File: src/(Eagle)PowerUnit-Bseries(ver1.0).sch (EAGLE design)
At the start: 84 parts, among them CON1 XT90PW-M, CON2 XT90PW-F, CON3 XT60PW-F, CON4 XT60PW-F, CON5 XT60PW-F, CON6 XT60PW-F, Q1 DMP3056L-7, Q3 DMP3056L-7, U1 LQFP64, U2 MCP2517FD, U3 CH340E, U4 AP63203WU-7, U5 AP63205WU-7, U6 AP331AWG-7, U8 AP331AWG-7

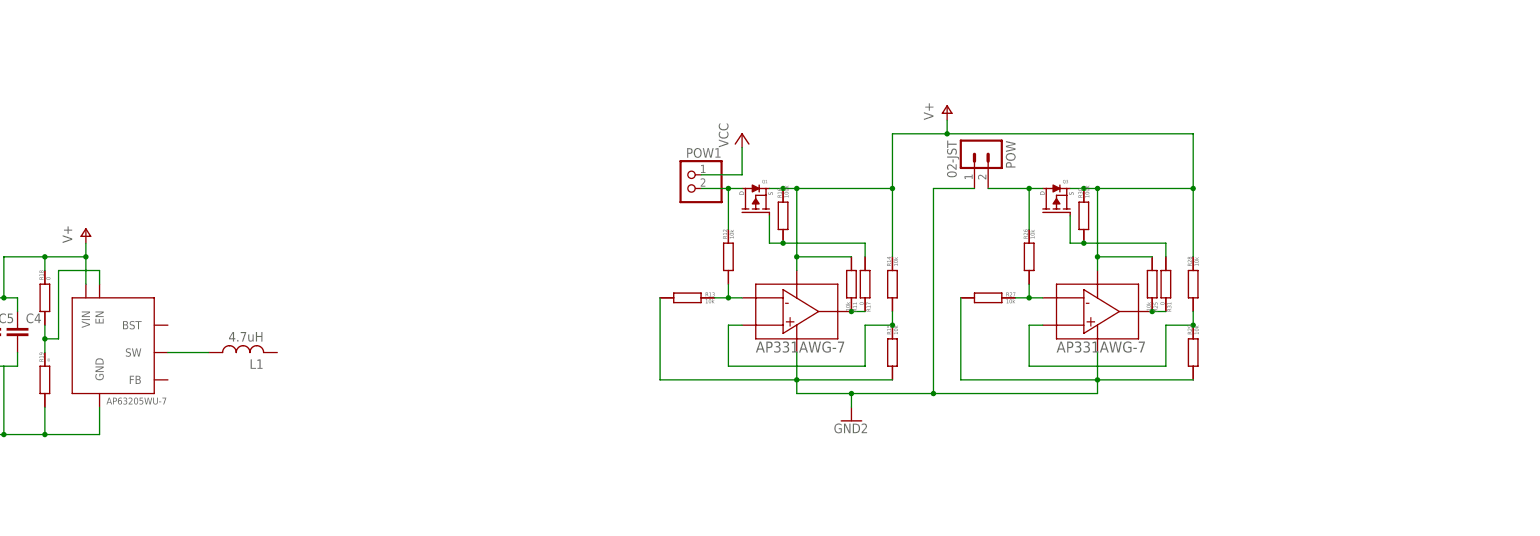
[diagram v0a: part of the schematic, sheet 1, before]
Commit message: 5VDCDCの出力コンをOSコンにした
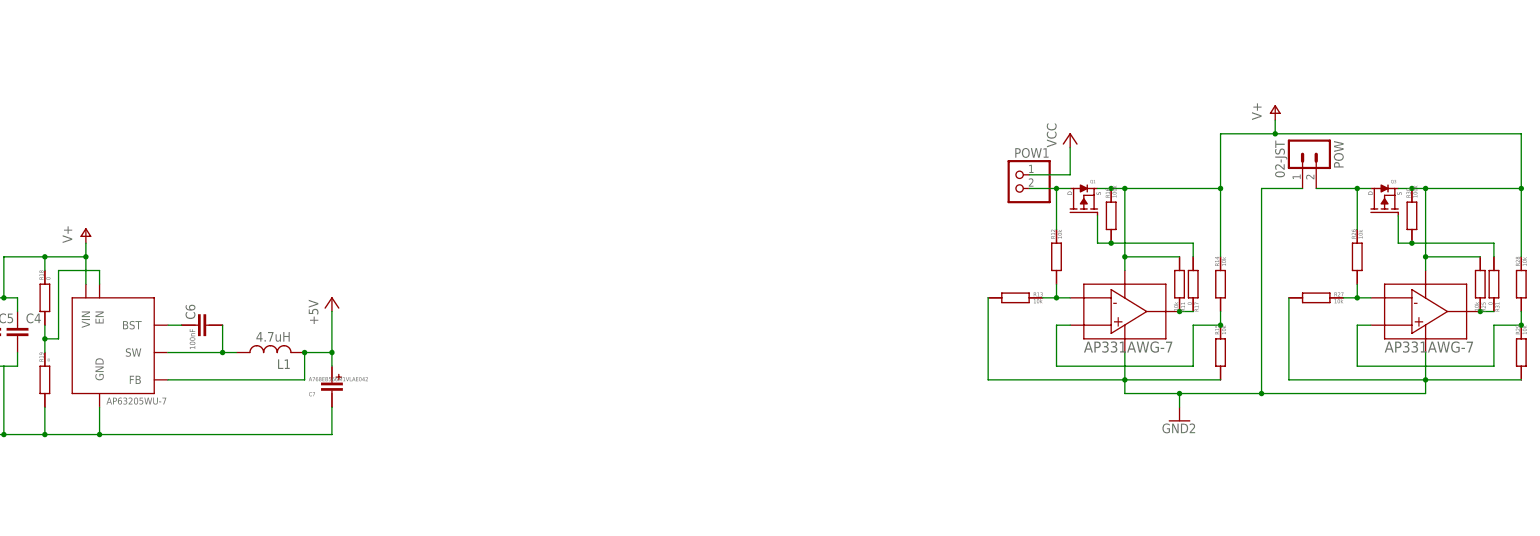
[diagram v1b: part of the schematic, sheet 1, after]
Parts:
- added C6: GCM188L81H104KA57, GCM188L81H104K57(0.1uF):GCM188L81H104KA57
- added C7: A768EB566M1VLAE042, A768EB566M1VLAE042:A768EB566M1VLAE042
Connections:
- new net +5V: C7.ANODE, L1.R, U5.FB
- new net N$41: C6.P$1, U5.BST
- net GND2: now also C7.CATHODE
- net N$40: now also C6.P$2
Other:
- moved on the sheet: L1, POW, POW1, Q1, Q3, R11, R12, R13, R14, R15, R16, R17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

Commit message: +5V周りの冗長性を高める回路を構成(大晦日ですよ？（笑）)
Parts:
- added C8: GCM188L81H104KA57, GCM188L81H104K57(0.1uF):GCM188L81H104KA57
- added Q2, Q4: SSM3J332R, SSM3J332R:SSM3J332R
- added R20, R21, R22, R23, R24, R34, R35, R36, R37, R38: 10k, CR0603:CR0603
- added R32, R39: 100k, CR0603:CR0603
- added R33, R40: 0, CR0603:CR0603
- added U7, U9: AP331AWG-7, AP331AWG-7:AP331AWG-7
- R18: value 0 -> 12k
- R19: value ∞ -> 3k
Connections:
- new net N$43: Q2.GATE, R20.RIGHT, R32.LEFT, R33.LEFT, R33.RIGHT, U7.OUTPUT
- new net N$44: R21.LEFT, R22.RIGHT, U7.IN-
- new net N$47: R23.LEFT, R24.RIGHT, U7.IN+
- new net N$51: Q4.GATE, R34.RIGHT, R39.LEFT, R40.LEFT, R40.RIGHT, U9.OUTPUT
- new net N$52: R35.LEFT, R36.RIGHT, U9.IN-
- new net N$53: R37.LEFT, R38.RIGHT, U9.IN+
- new net N$55: C7.ANODE, L1.R, Q2.DRAIN, R21.RIGHT, U5.FB
- net +5V: now also Q2.SOURCE, Q4.SOURCE, R20.LEFT, R23.RIGHT, R32.RIGHT, R34.LEFT, R37.RIGHT, R39.RIGHT, U7.VCC, U9.VCC; no longer C7.ANODE, L1.R, U5.FB
- net GND2: now also C8.P$2, R22.LEFT, R24.LEFT, R36.LEFT, R38.LEFT, U7.GND, U9.GND
- net U5V: now also Q4.DRAIN, R35.RIGHT
- net V+: now also C8.P$1
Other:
- moved on the sheet: C4, C5, GND, POW, POW1, Q1, Q3, R11, R12, R13, R14, R15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

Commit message: CANコントローラのXtal選定
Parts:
- removed JP2: (no value), pinhead:PINHD-1X2
- removed Q1, Q3: DMP3056L-7, DMP3056L-7:DMP3056L-7
- removed R11, R12, R13, R14, R15, R25, R26, R27, R28, R29: 10k, CR0603:CR0603
- removed R16, R30: 100k, CR0603:CR0603
- removed R17, R31: 0, CR0603:CR0603
- removed U4: AP63203WU-7, AP63203WU-7:AP63203WU-7
- removed U6, U8: AP331AWG-7, AP331AWG-7:AP331AWG-7
- added C10, C11, C13: GCM188L81H104KA57, GCM188L81H104K57(0.1uF):GCM188L81H104KA57
- added C12, C9: GRM32ER71E226KE15, GRM32ER71E226KE15:GRM32ER71E226KE15
- added D1, D2: GS1010FL, GS1010FL:GS1010FL
- added SW1: SS-12SDP2, SS-12SDP2:SS-12SDP2
- added U$4: AZ1117CH-3.3TRG1, AZ1117CH-3.3TRG1:AZ1117CH-3.3TRG1
- added X1: XRCGB40M000F4M00R0, XRCGB40M000F4M00R0:XRCGB40M000F4M00R0
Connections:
- removed net N$38 (its old number): R12.LEFT, R13.RIGHT, U6.IN-
- removed net N$45: POW.2, Q3.DRAIN, R26.RIGHT
- removed net N$46: Q3.GATE, R25.RIGHT, R30.LEFT, R31.LEFT, R31.RIGHT, U8.OUTPUT
- removed net N$48: R26.LEFT, R27.RIGHT, U8.IN-
- removed net N$49: R28.LEFT, R29.RIGHT, U8.IN+
- new net CS: U1.P33, U2.NCS
- new net MISO: U1.P35, U2.SDO
- new net MOSI: U1.P36, U2.SDI
- new net N$42: U2.OSC2, X1.1
- new net SCK: U1.P34, U2.SCK
- net +3V3: now also C11.P$1, C12.1, C13.P$2, U$1.VIO, U$4.OUTPUT, U2.VDD
- net +5V: now also C10.P$1, C9.1, U$1.VDD, U$4.INPUT
- net CANL: now also SW1.C; no longer JP2.2
- net GND: no longer U$1.VSS, U2.VSS
- net GND2: now also C10.P$2, C11.P$2, C12.2, C13.P$1, C9.2, U$1.VSS, U$4.GND, U2.VSS; no longer R13.LEFT, R15.LEFT, R27.LEFT, R29.LEFT, U4.GND, U6.GND, U8.GND
- net N$23: now also SW1.R; no longer JP2.1
- net N$35: now also D1.A; no longer Q1.DRAIN, R12.RIGHT
- net N$37: now also D2.A, POW.2; no longer Q1.GATE, R11.RIGHT, R16.LEFT, R17.LEFT, R17.RIGHT, U6.OUTPUT
- net N$39: now also U2.OSC1, X1.2; no longer R14.LEFT, R15.RIGHT, U6.IN+
- net V+: now also D1.C, D2.C; no longer Q1.SOURCE, Q3.SOURCE, R11.LEFT, R14.RIGHT, R16.RIGHT, R25.LEFT, R28.RIGHT, R30.RIGHT, U6.VCC, U8.VCC
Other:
- moved on the sheet: C3, C4, C5, C6, C7, C8, ECHO, GND, L1, LED4, POW, POW1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

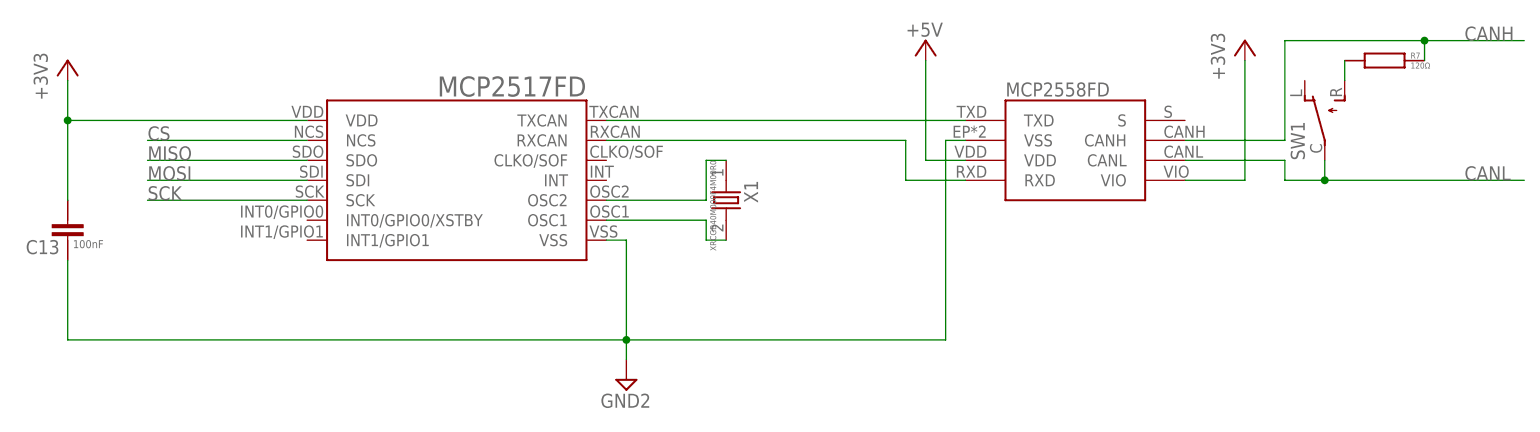
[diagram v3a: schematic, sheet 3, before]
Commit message: トランシーバ部分の設計終わり(仮)
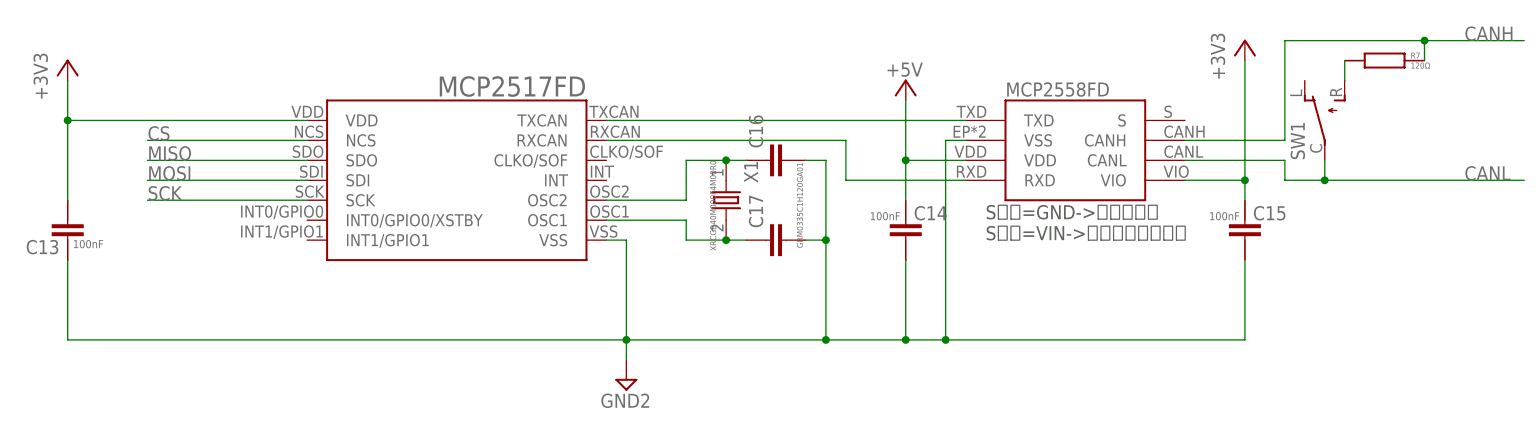
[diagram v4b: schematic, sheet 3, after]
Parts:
- added C14, C15: GCM188L81H104KA57, GCM188L81H104K57(0.1uF):GCM188L81H104KA57
- added C16, C17: GRM0335C1H120GA01, GRM0335C1H120GA01:GRM0335C1H120GA01
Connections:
- net +3V3: now also C15.P$1
- net +5V: now also C14.P$1
- net GND2: now also C14.P$2, C15.P$2, C16.2, C17.2
- net N$39: now also C17.1
- net N$42: now also C16.1
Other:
- note added: "Sピン=GND->通常モード Sピン=VIN->サイレントモード"
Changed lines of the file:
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@@
 <part name="P+12" library="supply1" library_urn="urn:adsk.eagle:library:371" deviceset="+5V" device=""/>
 <part name="+3V4" library="supply1" library_urn="urn:adsk.eagle:library:371" deviceset="+3V3" device=""/>
+<part name="C14" library="GCM188L81H104K57(0.1uF)" deviceset="GCM188L81H104KA57" device=""/>
+<part name="C15" library="GCM188L81H104K57(0.1uF)" deviceset="GCM188L81H104KA57" device=""/>
+<part name="C16" library="GRM0335C1H120GA01" deviceset="GRM0335C1H120GA01" device=""/>
+<part name="C17" library="GRM0335C1H120GA01" deviceset="GRM0335C1H120GA01" device=""/>
 </parts>
 <sheets>
@@
 <sheet>
 <plain>
+<text x="157.48" y="76.2" size="1.778" layer="97">Sピン=GND-&gt;通常モード
+Sピン=VIN-&gt;サイレントモード</text>
 </plain>
 <instances>
@@
 </instance>
 <instance part="X1" gate="G$1" x="124.46" y="81.28" smashed="yes" rot="R270">
-<attribute name="NAME" x="126.746" y="83.82" size="1.778" layer="95" rot="R270"/>
+<attribute name="NAME" x="126.746" y="86.36" size="1.778" layer="95" rot="R270"/>
 <attribute name="VALUE" x="123.19" y="86.36" size="0.762" layer="96" rot="MR270"/>
 </instance>
-<instance part="P+12" gate="1" x="149.86" y="101.6" smashed="yes"/>
+<instance part="P+12" gate="1" x="147.32" y="96.52" smashed="yes"/>
 <instance part="+3V4" gate="G$1" x="190.5" y="101.6" smashed="yes">
 <attribute name="VALUE" x="187.96" y="96.52" size="1.778" layer="96" rot="R90"/>
+</instance>
+<instance part="C14" gate="G$1" x="147.32" y="78.74" smashed="yes">
+<attribute name="NAME" x="148.336" y="78.74" size="1.778" layer="95"/>
+</instance>
+<instance part="C15" gate="G$1" x="190.5" y="78.74" smashed="yes">
+<attribute name="NAME" x="191.516" y="78.74" size="1.778" layer="95"/>
+</instance>
+<instance part="C16" gate="G$1" x="129.54" y="86.36" smashed="yes" rot="R90">
+<attribute name="NAME" x="129.159" y="87.884" size="1.778" layer="95" rot="R90"/>
+<attribute name="VALUE" x="134.239" y="75.184" size="0.762" layer="96" rot="R90"/>
+</instance>
+<instance part="C17" gate="G$1" x="129.54" y="76.2" smashed="yes" rot="R90">
+<attribute name="NAME" x="129.159" y="77.724" size="1.778" layer="95" rot="R90"/>
 </instance>
 </instances>
@@
 <segment>
 <pinref part="U2" gate="G$1" pin="RXCAN"/>
-<wire x1="109.22" y1="88.9" x2="147.32" y2="88.9" width="0.1524" layer="91"/>
-<wire x1="147.32" y1="88.9" x2="147.32" y2="83.82" width="0.1524" layer="91"/>
+<wire x1="109.22" y1="88.9" x2="139.7" y2="88.9" width="0.1524" layer="91"/>
+<wire x1="139.7" y1="88.9" x2="139.7" y2="83.82" width="0.1524" layer="91"/>
 <pinref part="U$1" gate="G$1" pin="RXD"/>
-<wire x1="147.32" y1="83.82" x2="154.94" y2="83.82" width="0.1524" layer="91"/>
+<wire x1="139.7" y1="83.82" x2="154.94" y2="83.82" width="0.1524" layer="91"/>
 </segment>
 </net>
@@
 <pinref part="+3V4" gate="G$1" pin="+3V3"/>
 <wire x1="190.5" y1="83.82" x2="190.5" y2="99.06" width="0.1524" layer="91"/>
+<pinref part="C15" gate="G$1" pin="P$1"/>
+<wire x1="190.5" y1="81.28" x2="190.5" y2="83.82" width="0.1524" layer="91"/>
+<junction x="190.5" y="83.82"/>
 </segment>
 </net>
@@
 <wire x1="40.64" y1="63.5" x2="111.76" y2="63.5" width="0.1524" layer="91"/>
 <junction x="111.76" y="63.5"/>
+<label x="108.458" y="54.864" size="1.778" layer="95"/>
+<pinref part="C14" gate="G$1" pin="P$2"/>
+<wire x1="147.32" y1="63.5" x2="137.16" y2="63.5" width="0.1524" layer="91"/>
+<wire x1="137.16" y1="63.5" x2="111.76" y2="63.5" width="0.1524" layer="91"/>
+<wire x1="147.32" y1="73.66" x2="147.32" y2="63.5" width="0.1524" layer="91"/>
+<junction x="147.32" y="63.5"/>
+<pinref part="C15" gate="G$1" pin="P$2"/>
+<wire x1="190.5" y1="73.66" x2="190.5" y2="63.5" width="0.1524" layer="91"/>
+<wire x1="190.5" y1="63.5" x2="152.4" y2="63.5" width="0.1524" layer="91"/>
 <pinref part="U$1" gate="G$1" pin="VSS"/>
+<wire x1="152.4" y1="63.5" x2="147.32" y2="63.5" width="0.1524" layer="91"/>
 <wire x1="154.94" y1="88.9" x2="152.4" y2="88.9" width="0.1524" layer="91"/>
 <wire x1="152.4" y1="88.9" x2="152.4" y2="63.5" width="0.1524" layer="91"/>
-<wire x1="152.4" y1="63.5" x2="111.76" y2="63.5" width="0.1524" layer="91"/>
-<label x="108.458" y="54.864" size="1.778" layer="95"/>
+<junction x="152.4" y="63.5"/>
+<pinref part="C17" gate="G$1" pin="2"/>
+<wire x1="134.62" y1="76.2" x2="137.16" y2="76.2" width="0.1524" layer="91"/>
+<wire x1="137.16" y1="76.2" x2="137.16" y2="86.36" width="0.1524" layer="91"/>
+<pinref part="C16" gate="G$1" pin="2"/>
+<wire x1="137.16" y1="86.36" x2="134.62" y2="86.36" width="0.1524" layer="91"/>
+<wire x1="137.16" y1="76.2" x2="137.16" y2="63.5" width="0.1524" layer="91"/>
+<junction x="137.16" y="76.2"/>
+<junction x="137.16" y="63.5"/>
 </segment>
 </net>
@@
 <segment>
 <pinref part="U2" gate="G$1" pin="OSC1"/>
-<wire x1="109.22" y1="78.74" x2="121.92" y2="78.74" width="0.1524" layer="91"/>
-<wire x1="121.92" y1="78.74" x2="121.92" y2="76.2" width="0.1524" layer="91"/>
+<wire x1="109.22" y1="78.74" x2="119.38" y2="78.74" width="0.1524" layer="91"/>
+<wire x1="119.38" y1="78.74" x2="119.38" y2="76.2" width="0.1524" layer="91"/>
 <pinref part="X1" gate="G$1" pin="2"/>
-<wire x1="121.92" y1="76.2" x2="124.46" y2="76.2" width="0.1524" layer="91"/>
+<wire x1="119.38" y1="76.2" x2="124.46" y2="76.2" width="0.1524" layer="91"/>
+<pinref part="C17" gate="G$1" pin="1"/>
+<wire x1="127" y1="76.2" x2="124.46" y2="76.2" width="0.1524" layer="91"/>
+<junction x="124.46" y="76.2"/>
 </segment>
 </net>
@@
 <segment>
 <pinref part="U2" gate="G$1" pin="OSC2"/>
-<wire x1="109.22" y1="81.28" x2="121.92" y2="81.28" width="0.1524" layer="91"/>
-<wire x1="121.92" y1="81.28" x2="121.92" y2="86.36" width="0.1524" layer="91"/>
+<wire x1="109.22" y1="81.28" x2="119.38" y2="81.28" width="0.1524" layer="91"/>
+<wire x1="119.38" y1="81.28" x2="119.38" y2="86.36" width="0.1524" layer="91"/>
 <pinref part="X1" gate="G$1" pin="1"/>
-<wire x1="121.92" y1="86.36" x2="124.46" y2="86.36" width="0.1524" layer="91"/>
+<wire x1="119.38" y1="86.36" x2="124.46" y2="86.36" width="0.1524" layer="91"/>
+<pinref part="C16" gate="G$1" pin="1"/>
+<wire x1="127" y1="86.36" x2="124.46" y2="86.36" width="0.1524" layer="91"/>
+<junction x="124.46" y="86.36"/>
 </segment>
 </net>
@@
 <segment>
 <pinref part="P+12" gate="1" pin="+5V"/>
-<label x="147.32" y="102.108" size="1.778" layer="95"/>
-<wire x1="149.86" y1="99.06" x2="149.86" y2="86.36" width="0.1524" layer="91"/>
+<label x="144.78" y="97.028" size="1.778" layer="95"/>
+<wire x1="147.32" y1="93.98" x2="147.32" y2="86.36" width="0.1524" layer="91"/>
 <pinref part="U$1" gate="G$1" pin="VDD"/>
-<wire x1="149.86" y1="86.36" x2="154.94" y2="86.36" width="0.1524" layer="91"/>
+<pinref part="C14" gate="G$1" pin="P$1"/>
+<wire x1="147.32" y1="86.36" x2="154.94" y2="86.36" width="0.1524" layer="91"/>
+<wire x1="147.32" y1="81.28" x2="147.32" y2="86.36" width="0.1524" layer="91"/>
+<junction x="147.32" y="86.36"/>
 </segment>
 </net>
@@
 </drawing>
 <compatibility>
+<note version="6.3" minversion="6.2.2" severity="warning">
+Since Version 6.2.2 text objects can contain more than one line,
+which will not be processed correctly with this version.
+</note>
 <note version="8.2" severity="warning">
 Since Version 8.2, EAGLE supports online libraries. The ids

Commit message: STM32の電源回り
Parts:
- added C18, C19, C20, C21: GCM188L81H104KA57, GCM188L81H104K57(0.1uF):GCM188L81H104KA57
- added R11: 10k, CR0603:CR0603
- added STLINK: (no value), con-jst-xh:06-JST
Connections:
- new net N$45: R11.LEFT, U1.P60
- new net NRST: STLINK.2, U1.P7
- new net SWCLK: STLINK.5, U1.P49
- new net SWDIO: STLINK.3, U1.P46
- new net SWO: STLINK.1, U1.P55
- net +3V3: now also C18.P$1, C19.P$1, C20.P$1, C21.P$1, STLINK.6, U1.P19, U1.P32, U1.P48, U1.P64
- net DIR1: now also U1.P24
- net DIR2: now also U1.P25
- net DIR3: now also U1.P26
- net DIR4: now also U1.P27
- net GND: now also C3.P$1, EDGE1.P24, EDGE2.P24, EDGE3.P24, EDGE4.P24, LED2.C, STLINK.4
- net GND2: now also C18.P$2, C19.P$2, C20.P$2, C21.P$2, R11.RIGHT, U1.P18, U1.P31, U1.P47, U1.P63; no longer C3.P$1, EDGE1.P24, EDGE2.P24, EDGE3.P24, EDGE4.P24, LED2.C
- net PWM1: now also U1.P50
- net PWM2: now also U1.P15
- net PWM3: now also U1.P29
- net PWM4: now also U1.P28
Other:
- note added: "BOOTモード->BOOT0=1,BOOT1=0"

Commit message: OSC周り
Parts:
- added B1: CS11029.5F100, CS11029.5F100:CS11029.5F100
- added BOOTMODE: (no value), pinhead:PINHD-1X2
- added C22, C25, C26: GCM188L81H104KA57, GCM188L81H104K57(0.1uF):GCM188L81H104KA57
- added C23: GRM21BC72A105KE01, GRM21BC72A105KE01(1uF):GRM21BC72A105KE01
- added C24: GRM31CR71H475KA12, GRM31CR71H475KA12:GRM31CR71H475KA12
- added FB1: BLM18KG121TN1D, BLM18KG121TN1D:BLM18KG121TN1D
- added R12, R13: 2.4Meg, CR0603:CR0603
- added R14, R16, R17, R25, R26: 0, CR0603:CR0603
- added R15: 100k, CR0603:CR0603
- added X2: RH100-24.000-18-1020-EXT-TR, RH100-24.000-18-1020-EXT-TR:RH100-24.000-18-1020-EXT-TR
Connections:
- net N$38 renamed VM2
- net N$44 renamed VM1
- new net BOOT0: BOOTMODE.1, R11.LEFT, U1.P60
- new net DIP_SW3: R25.RIGHT, U1.P52
- new net DIP_SW4: R26.RIGHT, U1.P51
- new net N$38: R14.LEFT, U2.OSC2
- new net N$44: R16.LEFT, U1.P16
- new net N$46: C22.P$1, C23.P$1, FB1.2, U1.P13
- new net N$48: C24.1, U1.P30
- new net N$49: U1.P5, X2.1
- new net N$50: U1.P6, X2.2
- net +3V3: now also BOOTMODE.2, C25.P$1, FB1.1, U1.P1
- net GND2: now also B1.3, C22.P$2, C23.P$2, C24.2, C25.P$2, C26.P$1, C26.P$2, R15.LEFT, U1.P12, X2.SHIELD
- net N$42: now also R14.RIGHT; no longer U2.OSC2
- net N$43: now also R12.LEFT
- net N$45: now also R17.LEFT, U1.P17; no longer R11.LEFT, U1.P60
- net N$47: now also R12.RIGHT
- net N$51: now also R13.LEFT
- net N$53: now also R13.RIGHT
- net NRST: now also B1.1
- net PWM4: now also R15.RIGHT
- net USART_RX: now also R17.RIGHT, R26.LEFT; no longer U1.P17
- net USART_TX: now also R16.RIGHT, R25.LEFT; no longer U1.P16
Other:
- note added: "BOOT"
- moved on the sheet: C10, C11, C12, C16, C17, C18, C19, C20, C21, C9, Q2, Q4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

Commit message: DIPスイッチ周り
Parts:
- added C27, C28: GRM0335C1E240GA01D, GRM0335C1E240GA01D:GRM0335C1E240GA01D
- added C29, C30: GRM0335C1H150FA01D, GRM0335C1H150FA01D:GRM0335C1H150FA01D
- added C31, C32, C33, C34: GCM188L81H104KA57, GCM188L81H104K57(0.1uF):GCM188L81H104KA57
- added JP2, JP3, JP4, JP5: (no value), con-jst-xh:05-JST
- added R27, R28: 0, CR0603:CR0603
- added R29, R30, R31, R41: 10k, CR0603:CR0603
- added SW2: RDS-16S-1055-SMT-TR, RDS-16S-1055-SMT-TR:RDS-16S-1055-SMT-TR
- added X3: 32.768K12.5PI/MC306, 32.768K12.5PI:32.768K12.5PI/MC306
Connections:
- new net DIP_SW1: R41.RIGHT, SW2.1
- new net DIP_SW2: R31.RIGHT, SW2.2
- new net ENC1_A: JP2.3, U1.P41
- new net ENC1_B: JP2.5, U1.P42
- new net ENC2_A: JP4.3, U1.P22
- new net ENC2_B: JP4.5, U1.P23
- new net ENC3_A: JP3.3, U1.P58
- new net ENC3_B: JP3.5, U1.P59
- new net ENC4_A: JP5.3, U1.P37
- new net ENC4_B: JP5.5, U1.P38
- new net N$52: R27.RIGHT, U1.P6
- new net N$54: C28.2, R27.LEFT, X2.2
- new net N$56: C30.2, R28.LEFT, X3.1
- new net N$57: C29.2, U1.P3, X3.2
- net +3V3: now also SW2.C
- net +5V: now also C31.P$1, C32.P$1, C33.P$1, C34.P$1, JP2.4, JP3.4, JP4.4, JP5.4
- net DIP_SW3: now also R30.RIGHT, SW2.4
- net DIP_SW4: now also R29.RIGHT, SW2.8
- net GND2: now also C27.1, C28.1, C29.1, C30.1, C31.P$2, C32.P$2, C33.P$2, C34.P$2, JP2.1, JP3.1, JP4.1, JP5.1, R29.LEFT, R30.LEFT, R31.LEFT, R41.LEFT
- net N$49: now also C27.2
- net N$50: now also R28.RIGHT, U1.P4; no longer U1.P6, X2.2
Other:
- moved on the sheet: C1, C2, CON1, CON2, CON3, CON4, CON5, CON6, CTRL1, CTRL2, EDGE1, EDGE2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
